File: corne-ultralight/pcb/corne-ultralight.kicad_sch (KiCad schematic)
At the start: 110 parts, among them J2 OLED, J7 OLED, SW1 SW_PUSH, SW10 SW_PUSH, SW11 SW_PUSH, SW12 SW_PUSH, SW13 SW_PUSH, SW14 SW_PUSH, SW15 SW_PUSH, SW16 SW_PUSH, SW17 SW_PUSH, SW18 SW_PUSH, SW19 SW_PUSH, SW2 SW_PUSH, SW20 SW_PUSH, SW21 SW_PUSH, SW22 SW_PUSH, SW23 SW_PUSH, SW24 SW_PUSH, SW25 SW_PUSH, SW26 SW_PUSH, SW27 SW_PUSH, SW28 SW_PUSH, SW29 SW_PUSH, SW3 SW_PUSH, SW30 SW_PUSH, SW31 SW_PUSH, SW32 SW_PUSH, SW33 SW_PUSH, SW34 SW_PUSH, SW35 SW_PUSH, SW36 SW_PUSH, SW37 SW_PUSH, SW38 SW_PUSH, SW39 SW_PUSH, SW4 SW_PUSH, SW40 SW_PUSH, SW41 SW_PUSH, SW42 SW_PUSH, SW5 SW_PUSH, SW6 SW_PUSH, SW7 SW_PUSH, SW8 SW_PUSH, SW9 SW_PUSH, U1 ProMicro, U2 ProMicro

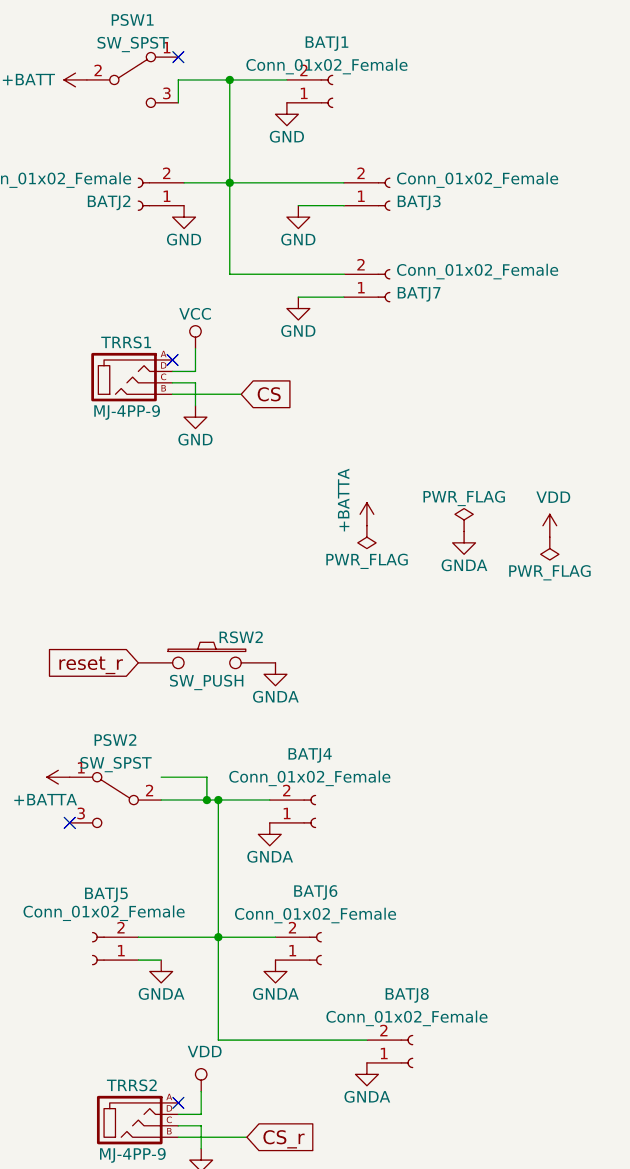
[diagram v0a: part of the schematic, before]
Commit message: Additional JST
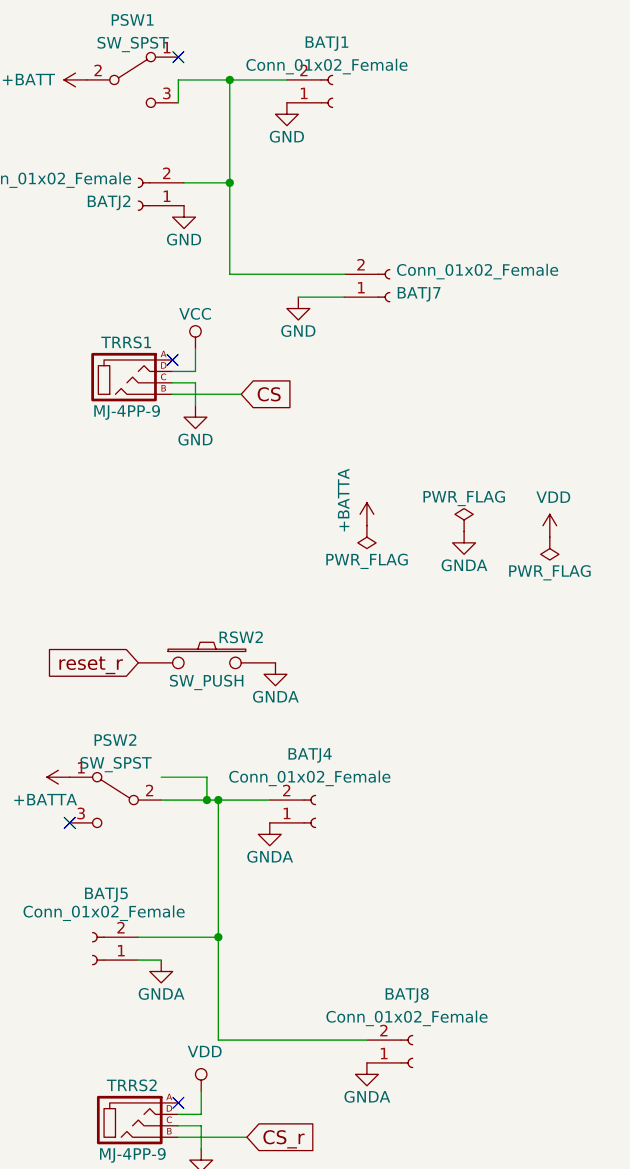
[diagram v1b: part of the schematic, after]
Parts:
- removed BATJ3, BATJ6: Conn_01x02_Female, Connector_JST:JST_PH_S2B-PH-K_1x02_P2.00mm_Horizontal, symbol Connector:Conn_01x02_Female

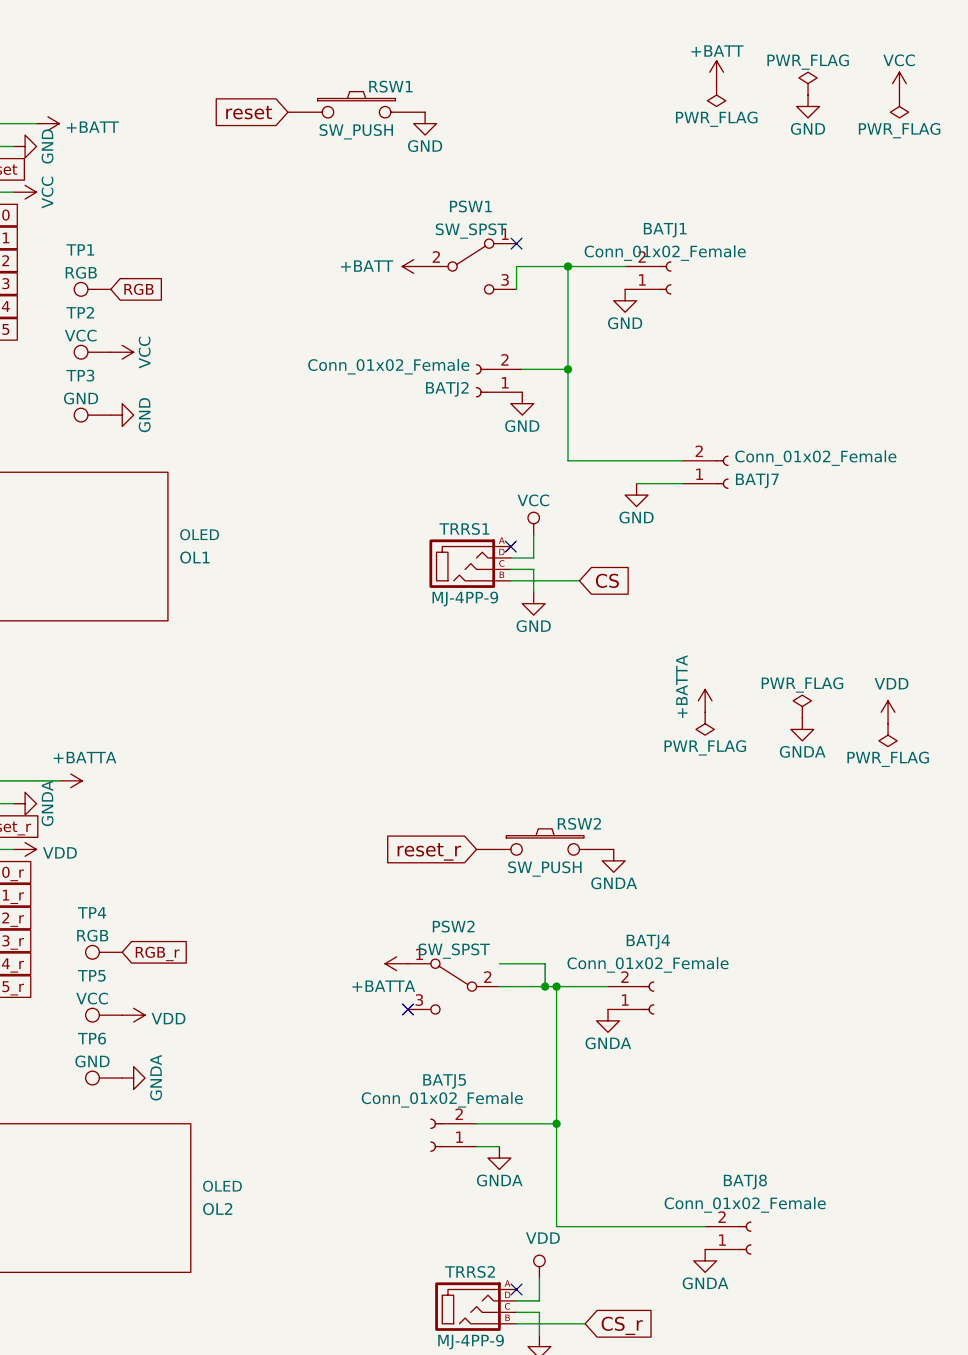
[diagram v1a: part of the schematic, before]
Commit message: Reversed power switches
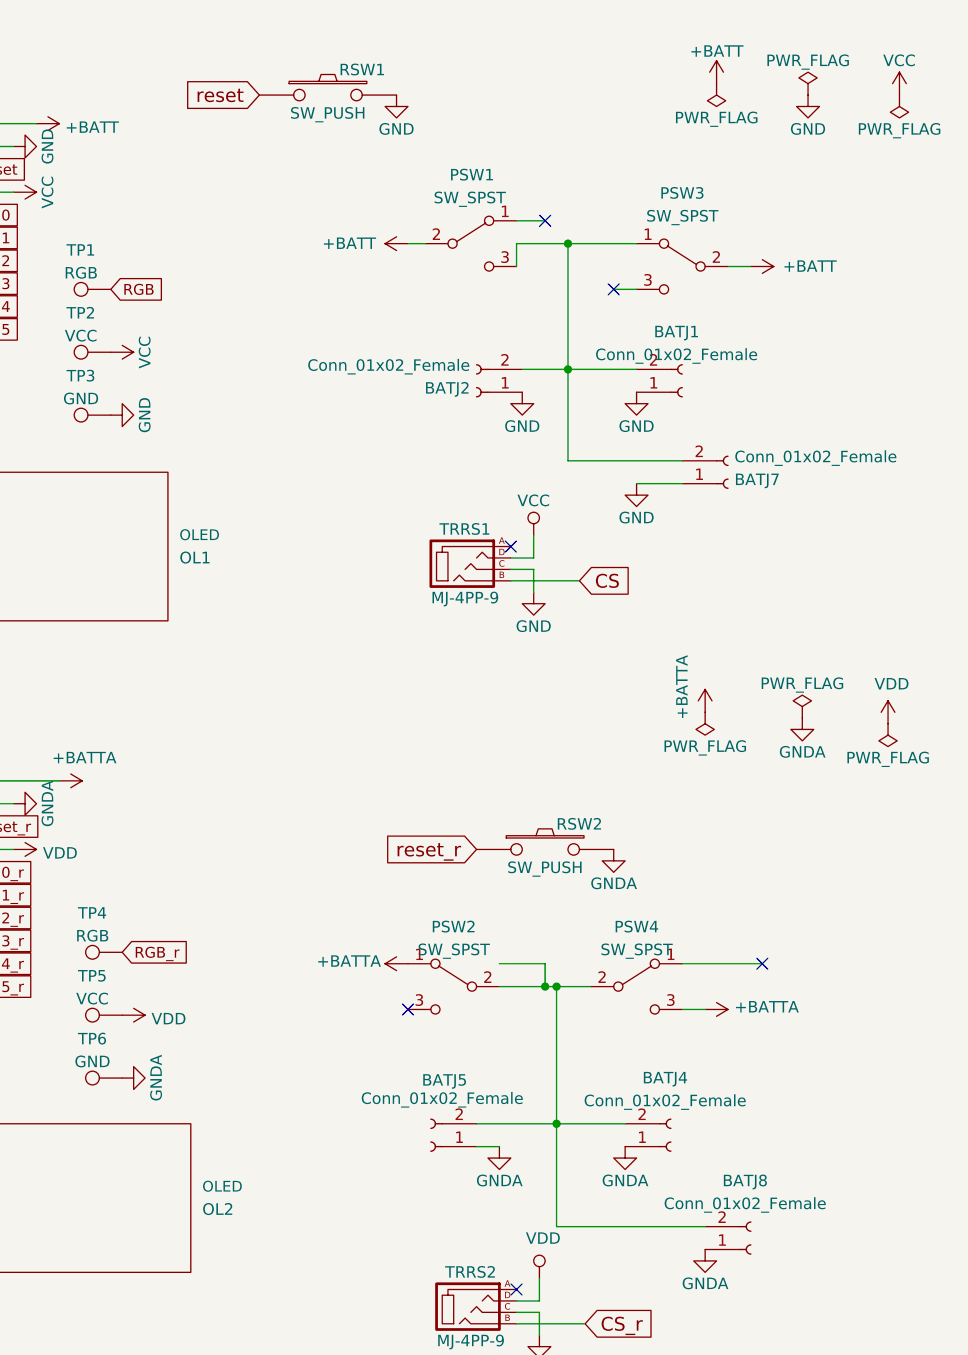
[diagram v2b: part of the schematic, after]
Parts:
- added PSW3, PSW4: SW_SPST, Button_Switch_SMD:SW_SPDT_PCM12, symbol Switch:SW_SPDT
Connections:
- net +BATT: now also PSW3.2 (B)
- net +BATTA: now also PSW4.3 (C)
- net at BATJ4.2 (Pin_2), BATJ5.2 (Pin_2), BATJ8.2 (Pin_2)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: now also PSW4.2 (B)
- net at BATJ1.2 (Pin_2), BATJ2.2 (Pin_2), BATJ7.2 (Pin_2)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: now also PSW3.1 (A)
- no-connect marks 12 -> 14
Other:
- moved on the sheet: BATJ1, BATJ4, PSW1, RSW1

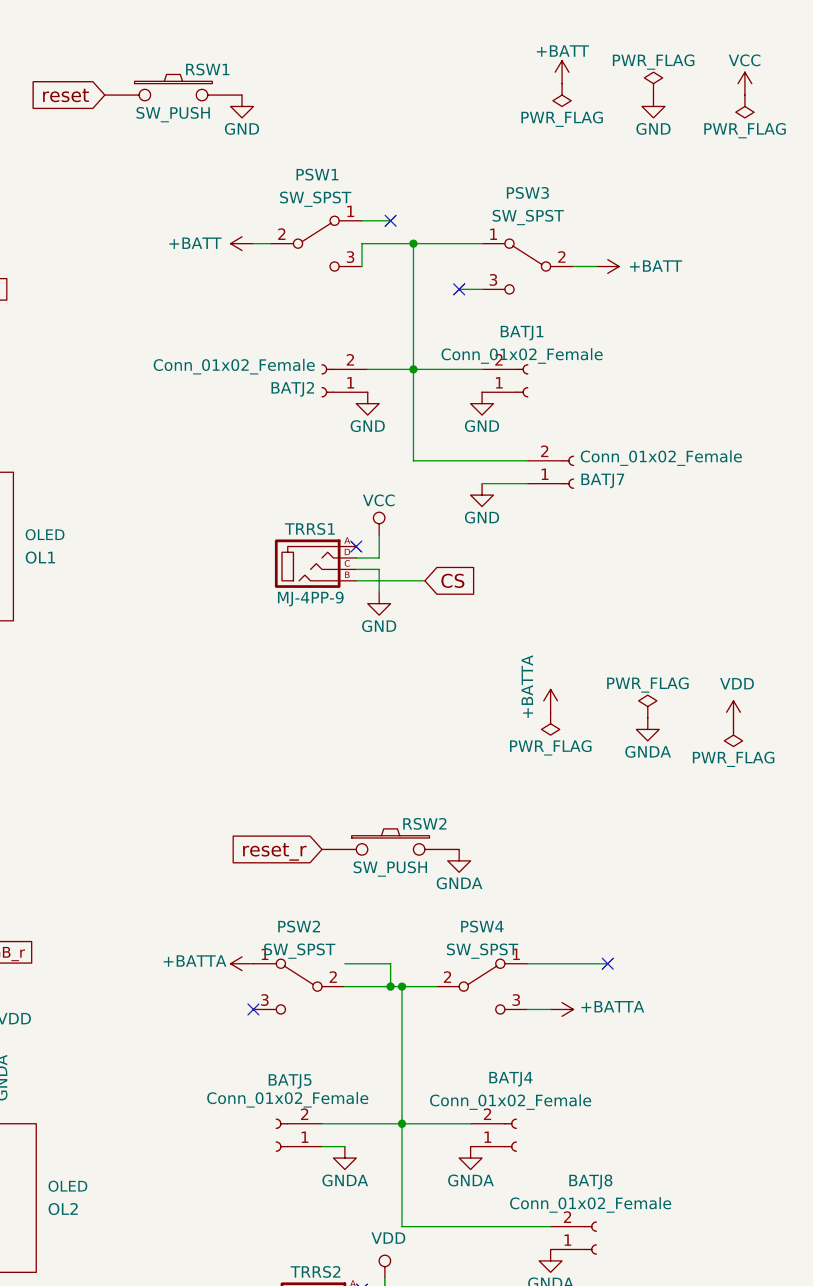
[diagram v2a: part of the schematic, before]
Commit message: Reversed power switches
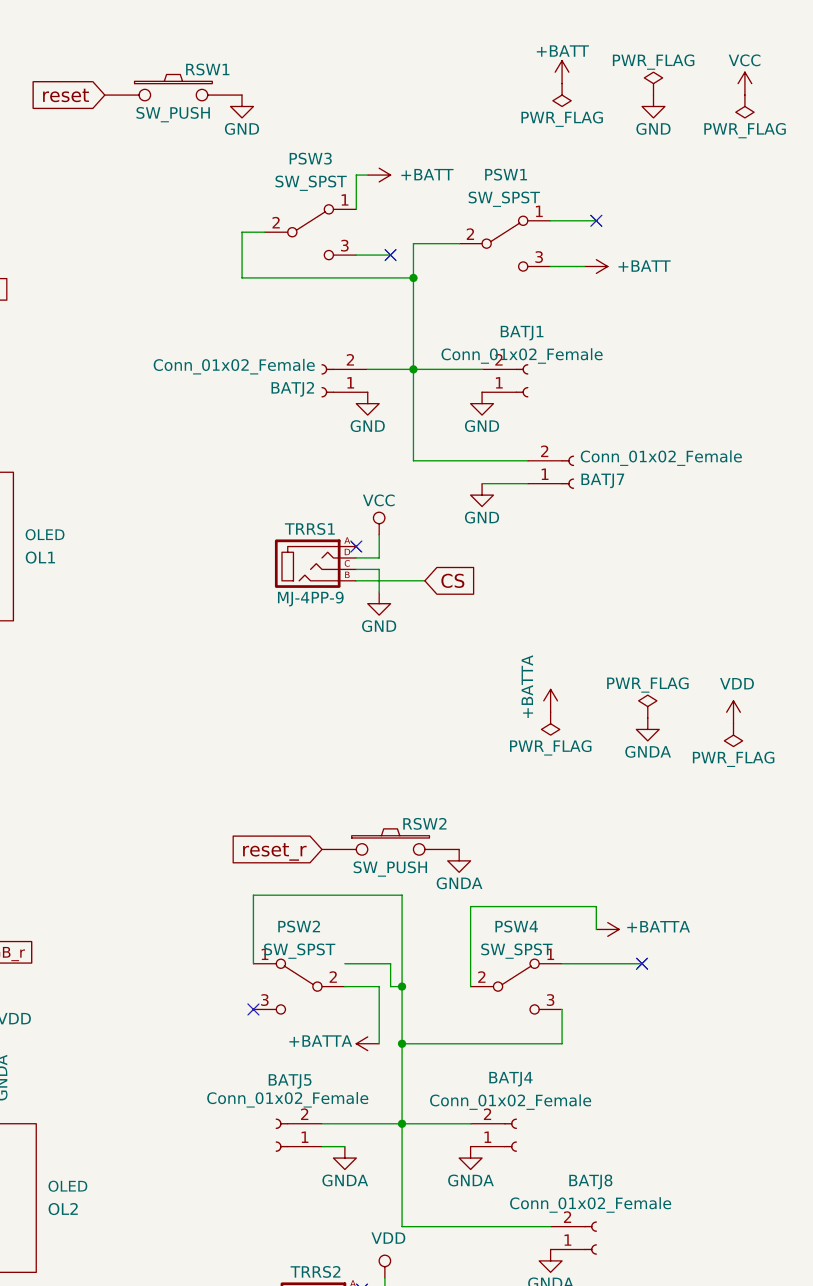
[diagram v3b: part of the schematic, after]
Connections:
- net +BATT: now also PSW1.3 (C), PSW3.1 (A); no longer PSW1.2 (B), PSW3.2 (B)
- net +BATTA: now also PSW2.2 (B), PSW4.2 (B); no longer PSW2.1 (A), PSW4.3 (C)
- net at BATJ4.2 (Pin_2), BATJ5.2 (Pin_2), BATJ8.2 (Pin_2): now also PSW2.1 (A), PSW4.3 (C); no longer PSW2.2 (B), PSW4.2 (B)
- net at BATJ1.2 (Pin_2), BATJ2.2 (Pin_2), BATJ7.2 (Pin_2): now also PSW1.2 (B), PSW3.2 (B); no longer PSW1.3 (C), PSW3.1 (A)
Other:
- moved on the sheet: PSW1, PSW3, PSW4

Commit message: tree pin reset btn WIP
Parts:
- added RSW3, RSW4: SW_PUSH, JxComponents:JxTreePinButton, symbol kbd:SW_PUSH
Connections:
- net GND: now also RSW3.2
- net GNDA: now also RSW4.1
- net reset: now also RSW3.1
- net reset_r: now also RSW4.2

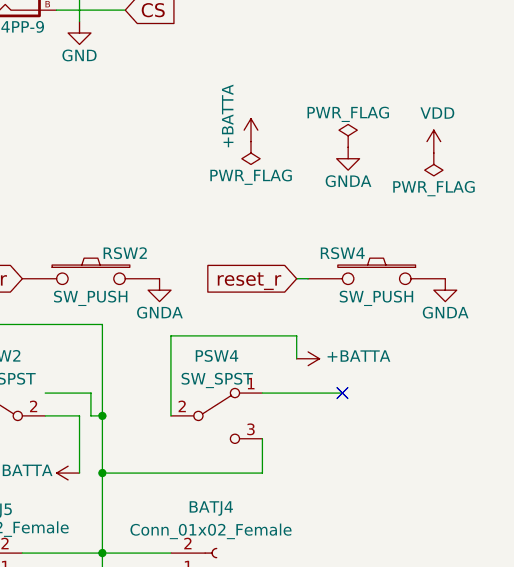
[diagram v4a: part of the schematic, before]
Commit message: tree pin reset btn. done.
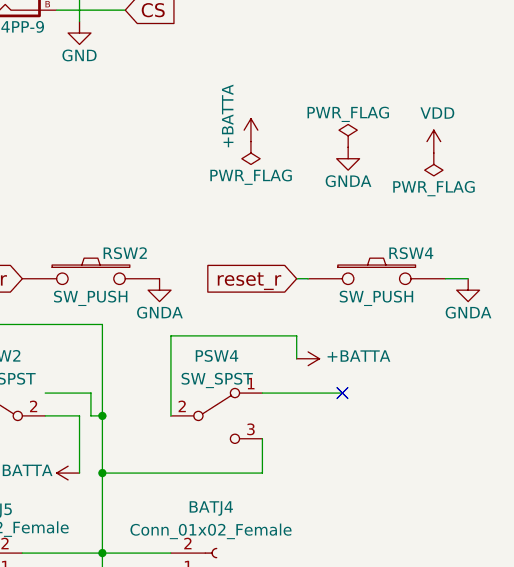
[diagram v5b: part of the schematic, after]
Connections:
- net GNDA: now also RSW4.2; no longer RSW4.1
- net reset_r: now also RSW4.1; no longer RSW4.2
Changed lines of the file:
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@@
 	(wire
 		(pts
-			(xy 262.89 102.87) (xy 264.16 102.87)
+			(xy 162.56 63.5) (xy 163.83 63.5)
 		)
 		(stroke
@@
 	(wire
 		(pts
-			(xy 162.56 63.5) (xy 163.83 63.5)
+			(xy 279.4 102.87) (xy 281.94 102.87)
 		)
 		(stroke
@@
 	(wire
 		(pts
+			(xy 262.89 102.87) (xy 264.16 102.87)
+		)
+		(stroke
+			(width 0)
+			(type default)
+		)
+	)
+	(wire
+		(pts
 			(xy 234.95 118.11) (xy 238.76 118.11)
 		)
@@
 		(lib_id "kbd:SW_PUSH")
 		(at 271.78 102.87 0)
-		(mirror y)
 		(unit 1)
 		(exclude_from_sim no)
@@
 		(dnp no)
 		(property "Reference" "RSW4"
-			(at 267.97 100.076 0)
+			(at 275.59 100.076 0)
 			(effects
 				(font
@@
 	(symbol
 		(lib_id "power:GNDA")
-		(at 279.4 102.87 0)
+		(at 281.94 102.87 0)
 		(unit 1)
 		(exclude_from_sim no)
@@
 		(dnp no)
 		(property "Reference" "#PWR029"
-			(at 279.4 109.22 0)
+			(at 281.94 109.22 0)
 			(effects
 				(font
@@
 		)
 		(property "Value" "GNDA"
-			(at 279.4 106.68 0)
+			(at 281.94 106.68 0)
 			(effects
 				(font
@@
 		)
 		(property "Footprint" ""
-			(at 279.4 102.87 0)
+			(at 281.94 102.87 0)
 			(effects
 				(font
@@
 		)
 		(property "Datasheet" ""
-			(at 279.4 102.87 0)
+			(at 281.94 102.87 0)
 			(effects
 				(font
@@
 		)
 		(property "Description" ""
-			(at 279.4 102.87 0)
+			(at 281.94 102.87 0)
 			(effects
 				(font
